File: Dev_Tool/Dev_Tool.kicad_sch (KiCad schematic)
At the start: 0 parts

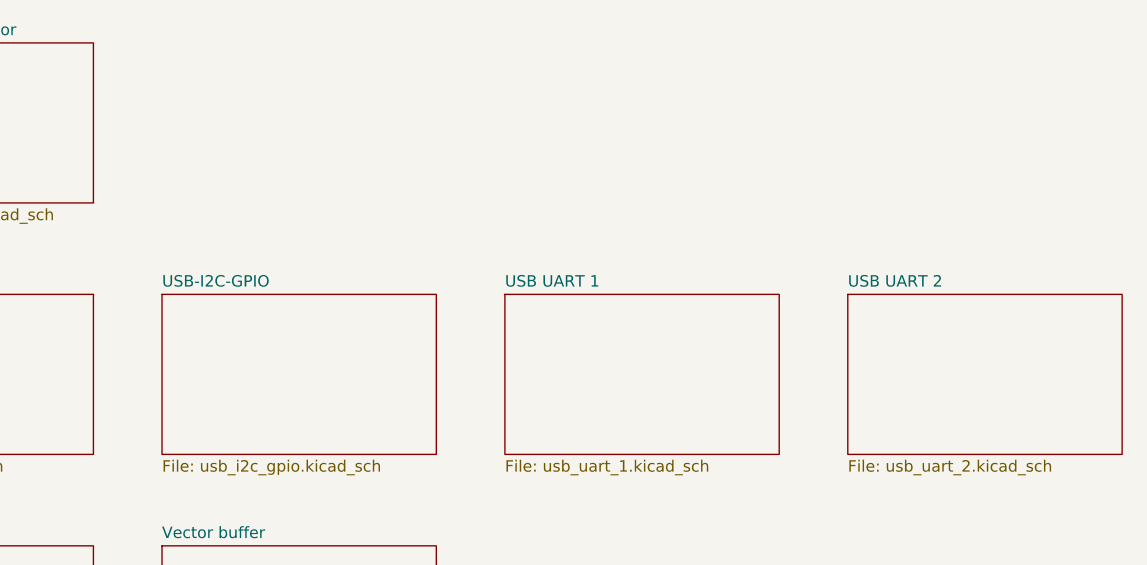
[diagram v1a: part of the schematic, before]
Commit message: Add unconnected pins to CPLD symbol
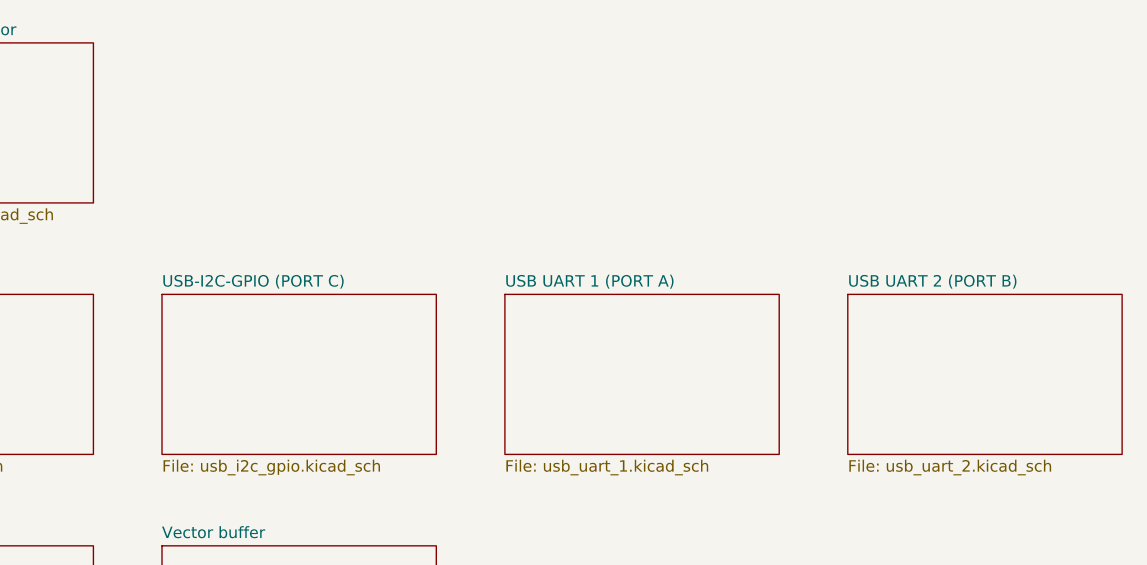
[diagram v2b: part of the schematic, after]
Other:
- sheet USB UART 1 renamed USB UART 1 (PORT A)
- sheet USB UART 2 renamed USB UART 2 (PORT B)
- sheet USB-I2C-GPIO renamed USB-I2C-GPIO (PORT C)
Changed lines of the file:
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@@
 	(title_block
 		(title "COMETbus DEVELOPMENT TOOL")
-		(date "2025-09-08")
+		(date "2025-09-09")
 		(rev "1")
 		(company "(C) TOM STOREY")
@@
 			(color 0 0 0 0.0000)
 		)
-		(property "Sheetname" "USB UART 2"
+		(property "Sheetname" "USB UART 2 (PORT B)"
 			(at 144.78 57.7084 0)
 			(effects
@@
 			(color 0 0 0 0.0000)
 		)
-		(property "Sheetname" "USB UART 1"
+		(property "Sheetname" "USB UART 1 (PORT A)"
 			(at 106.68 57.7084 0)
 			(effects
@@
 			(color 0 0 0 0.0000)
 		)
-		(property "Sheetname" "USB-I2C-GPIO"
+		(property "Sheetname" "USB-I2C-GPIO (PORT C)"
 			(at 68.58 57.7084 0)
 			(effects

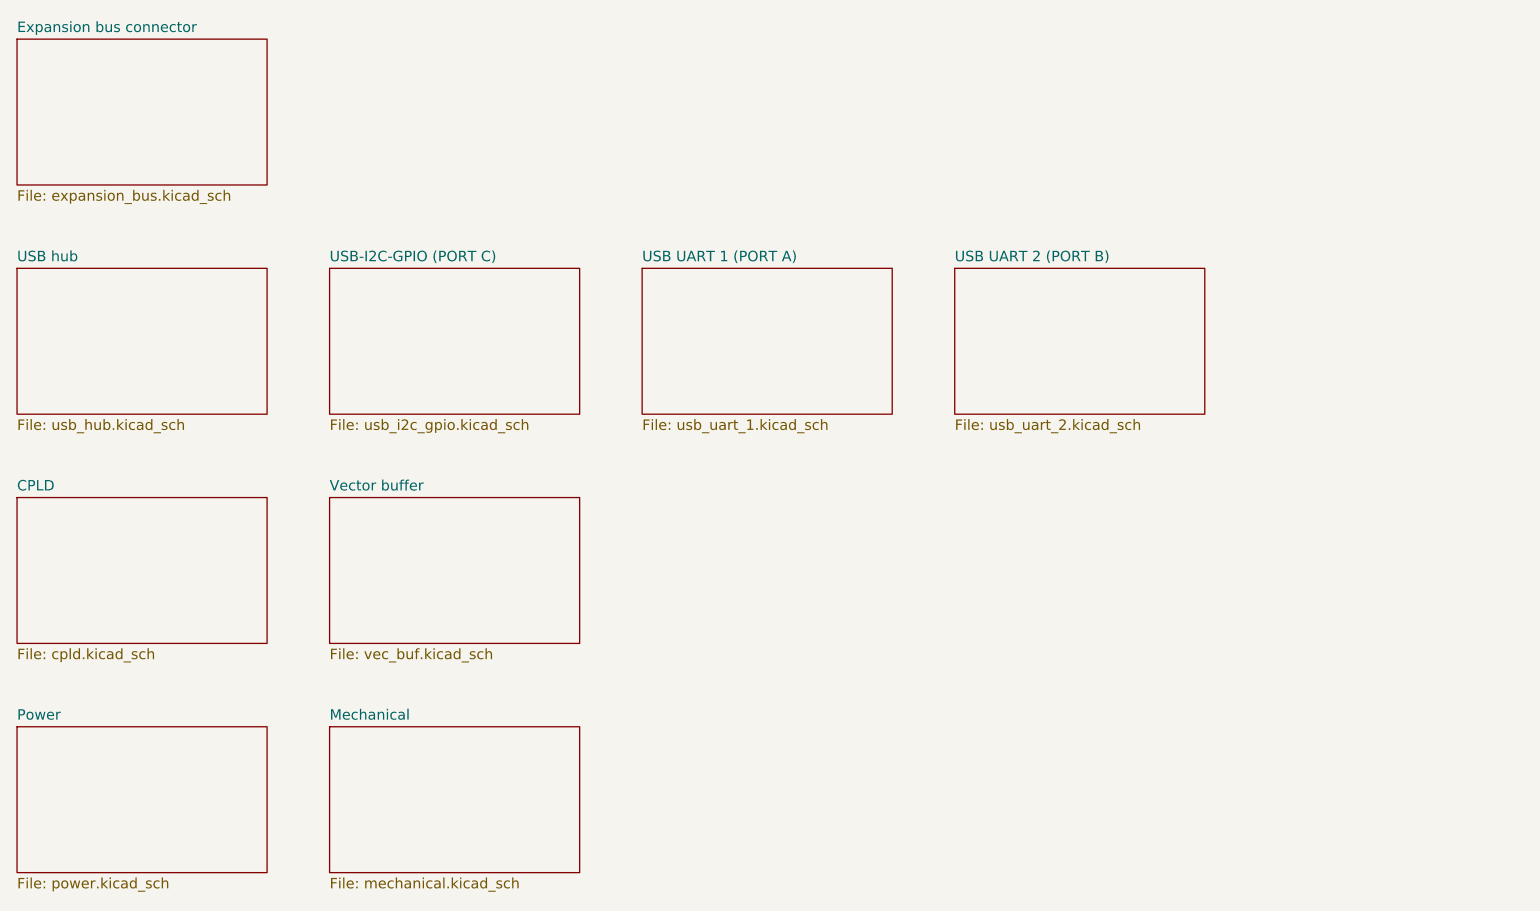
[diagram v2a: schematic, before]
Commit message: Rev 2 fixes
* R5/C1 reference silkscreens were swapped around
* LED logic for the PC LED was reverse to what I thought it would be, fixed by adding Q1
* Change DEV LED to PWR ON LED, since it comes on when the port is powered, not just when a device is connected. Switched via Q2 so it doesnt fade on power down.
* IN USE LED now comes off MCP2221A pin - the PCA9535 doesnt have a reset, so this LED could remain lit even after a reset.
* Pull up/down added to vector buffer
* 8P8C sockets moved further out as they are shorter than the footprint suggests
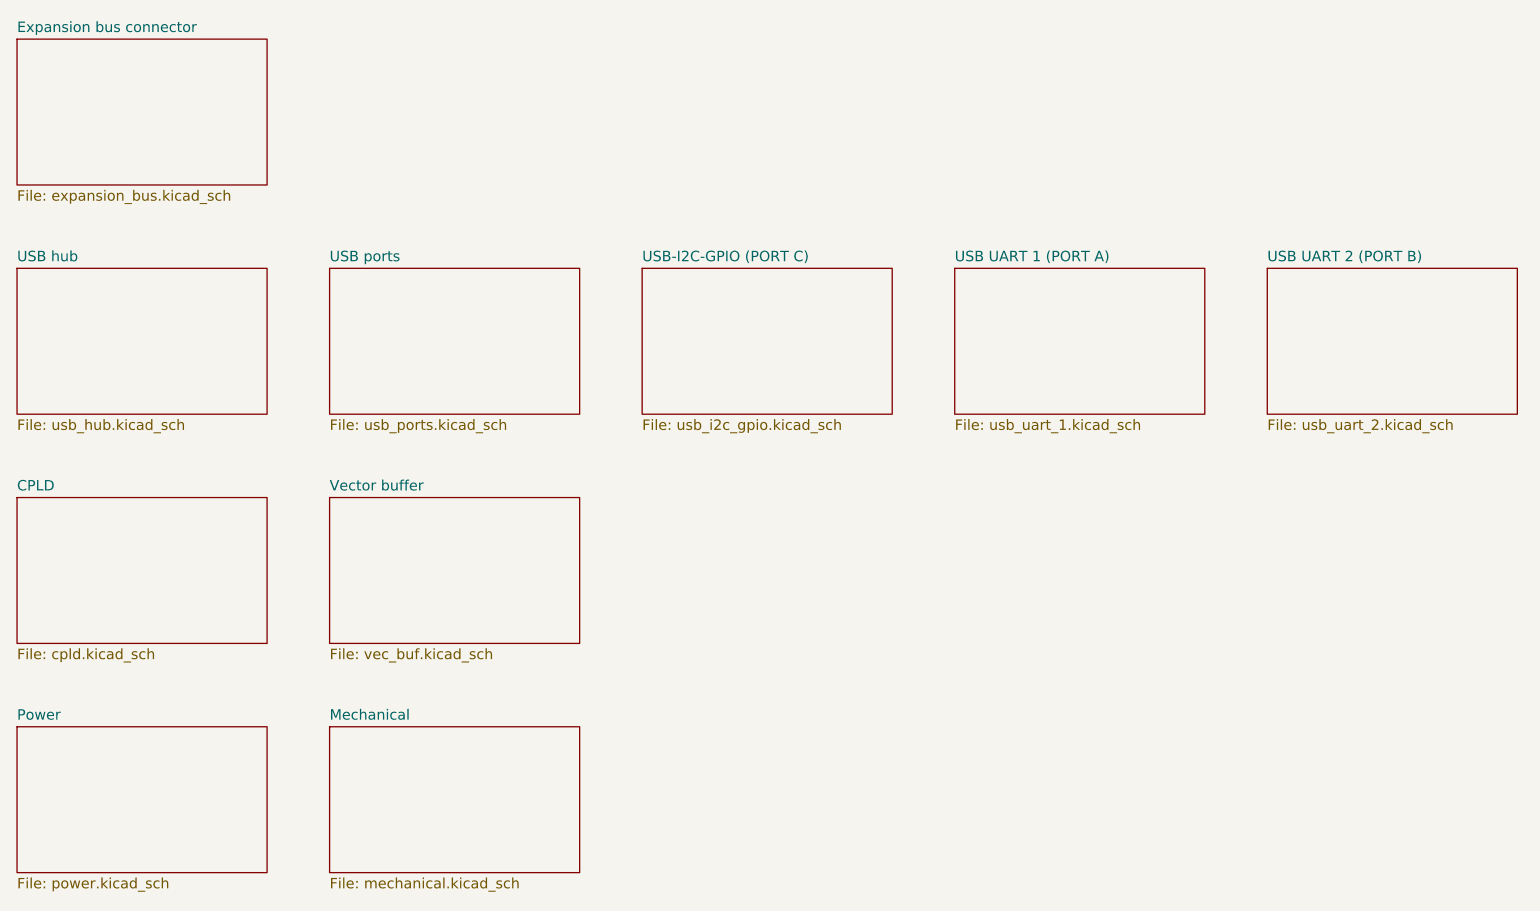
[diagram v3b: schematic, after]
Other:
- added sheet USB ports (usb_ports.kicad_sch)
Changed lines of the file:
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@@
 	(title_block
 		(title "COMETbus DEVELOPMENT TOOL")
-		(date "2025-09-09")
-		(rev "1")
+		(date "2025-09-18")
+		(rev "2")
 		(company "(C) TOM STOREY")
 		(comment 1 "FREE FOR NON-COMMERCIAL USE")
@@
 			(project "Dev_Tool"
 				(path "/a5cc9727-587c-40e3-bd55-82381bb9520b"
+					(page "8")
+				)
+			)
+		)
+	)
+	(sheet
+		(at 182.88 58.42)
+		(size 30.48 17.78)
+		(exclude_from_sim no)
+		(in_bom yes)
+		(on_board yes)
+		(dnp no)
+		(fields_autoplaced yes)
+		(stroke
+			(width 0.1524)
+			(type solid)
+		)
+		(fill
+			(color 0 0 0 0.0000)
+		)
+		(property "Sheetname" "USB UART 2 (PORT B)"
+			(at 182.88 57.7084 0)
+			(effects
+				(font
+					(size 1.27 1.27)
+				)
+				(justify left bottom)
+			)
+		)
+		(property "Sheetfile" "usb_uart_2.kicad_sch"
+			(at 182.88 76.7846 0)
+			(effects
+				(font
+					(size 1.27 1.27)
+				)
+				(justify left top)
+			)
+		)
+		(instances
+			(project "Dev_Tool"
+				(path "/a5cc9727-587c-40e3-bd55-82381bb9520b"
 					(page "7")
 				)
@@
 			(color 0 0 0 0.0000)
 		)
-		(property "Sheetname" "USB UART 2 (PORT B)"
+		(property "Sheetname" "USB UART 1 (PORT A)"
 			(at 144.78 57.7084 0)
 			(effects
@@
 			)
 		)
-		(property "Sheetfile" "usb_uart_2.kicad_sch"
+		(property "Sheetfile" "usb_uart_1.kicad_sch"
 			(at 144.78 76.7846 0)
 			(effects
@@
 				(path "/a5cc9727-587c-40e3-bd55-82381bb9520b"
 					(page "6")
-				)
-			)
-		)
-	)
-	(sheet
-		(at 106.68 58.42)
-		(size 30.48 17.78)
-		(exclude_from_sim no)
-		(in_bom yes)
-		(on_board yes)
-		(dnp no)
-		(fields_autoplaced yes)
-		(stroke
-			(width 0.1524)
-			(type solid)
-		)
-		(fill
-			(color 0 0 0 0.0000)
-		)
-		(property "Sheetname" "USB UART 1 (PORT A)"
-			(at 106.68 57.7084 0)
-			(effects
-				(font
-					(size 1.27 1.27)
-				)
-				(justify left bottom)
-			)
-		)
-		(property "Sheetfile" "usb_uart_1.kicad_sch"
-			(at 106.68 76.7846 0)
-			(effects
-				(font
-					(size 1.27 1.27)
-				)
-				(justify left top)
-			)
-		)
-		(instances
-			(project "Dev_Tool"
-				(path "/a5cc9727-587c-40e3-bd55-82381bb9520b"
-					(page "5")
 				)
 			)
@@
 			(project "Dev_Tool"
 				(path "/a5cc9727-587c-40e3-bd55-82381bb9520b"
-					(page "10")
+					(page "11")
 				)
 			)
@@
 			(project "Dev_Tool"
 				(path "/a5cc9727-587c-40e3-bd55-82381bb9520b"
-					(page "9")
+					(page "10")
 				)
 			)
@@
 			(project "Dev_Tool"
 				(path "/a5cc9727-587c-40e3-bd55-82381bb9520b"
-					(page "8")
-				)
-			)
-		)
-	)
-	(sheet
-		(at 68.58 58.42)
+					(page "9")
+				)
+			)
+		)
+	)
+	(sheet
+		(at 106.68 58.42)
 		(size 30.48 17.78)
 		(exclude_from_sim no)
@@
 		)
 		(property "Sheetname" "USB-I2C-GPIO (PORT C)"
-			(at 68.58 57.7084 0)
+			(at 106.68 57.7084 0)
 			(effects
 				(font
@@
 		)
 		(property "Sheetfile" "usb_i2c_gpio.kicad_sch"
-			(at 68.58 76.7846 0)
-			(effects
-				(font
-					(size 1.27 1.27)
-				)
-				(justify left top)
-			)
-		)
-		(instances
-			(project "Dev_Tool"
-				(path "/a5cc9727-587c-40e3-bd55-82381bb9520b"
-					(page "4")
+			(at 106.68 76.7846 0)
+			(effects
+				(font
+					(size 1.27 1.27)
+				)
+				(justify left top)
+			)
+		)
+		(instances
+			(project "Dev_Tool"
+				(path "/a5cc9727-587c-40e3-bd55-82381bb9520b"
+					(page "5")
 				)
 			)
@@
 				)
 			)
+		)
+	)
+	(sheet
+		(at 68.58 58.42)
+		(size 30.48 17.78)
+		(exclude_from_sim no)
+		(in_bom yes)
+		(on_board yes)
+		(dnp no)
+		(fields_autoplaced yes)
+		(stroke
+			(width 0.1524)
+			(type solid)
+		)
+		(fill
+			(color 0 0 0 0.0000)
+		)
+		(property "Sheetname" "USB ports"
+			(at 68.58 57.7084 0)
+			(effects
+				(font
+					(size 1.27 1.27)
+				)
+				(justify left bottom)
+			)
+		)
+		(property "Sheetfile" "usb_ports.kicad_sch"
+			(at 68.58 76.7846 0)
+			(effects
+				(font
+					(size 1.27 1.27)
+				)
+				(justify left top)
+			)
+		)
+		(instances
+			(project "Dev_Tool"
+				(path "/a5cc9727-587c-40e3-bd55-82381bb9520b"
+					(page "4")
+				)
+			)
